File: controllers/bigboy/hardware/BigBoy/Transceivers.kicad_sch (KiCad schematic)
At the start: 15 parts, among them U13 74ALVC16245DG, U8 74ALVC16245DG

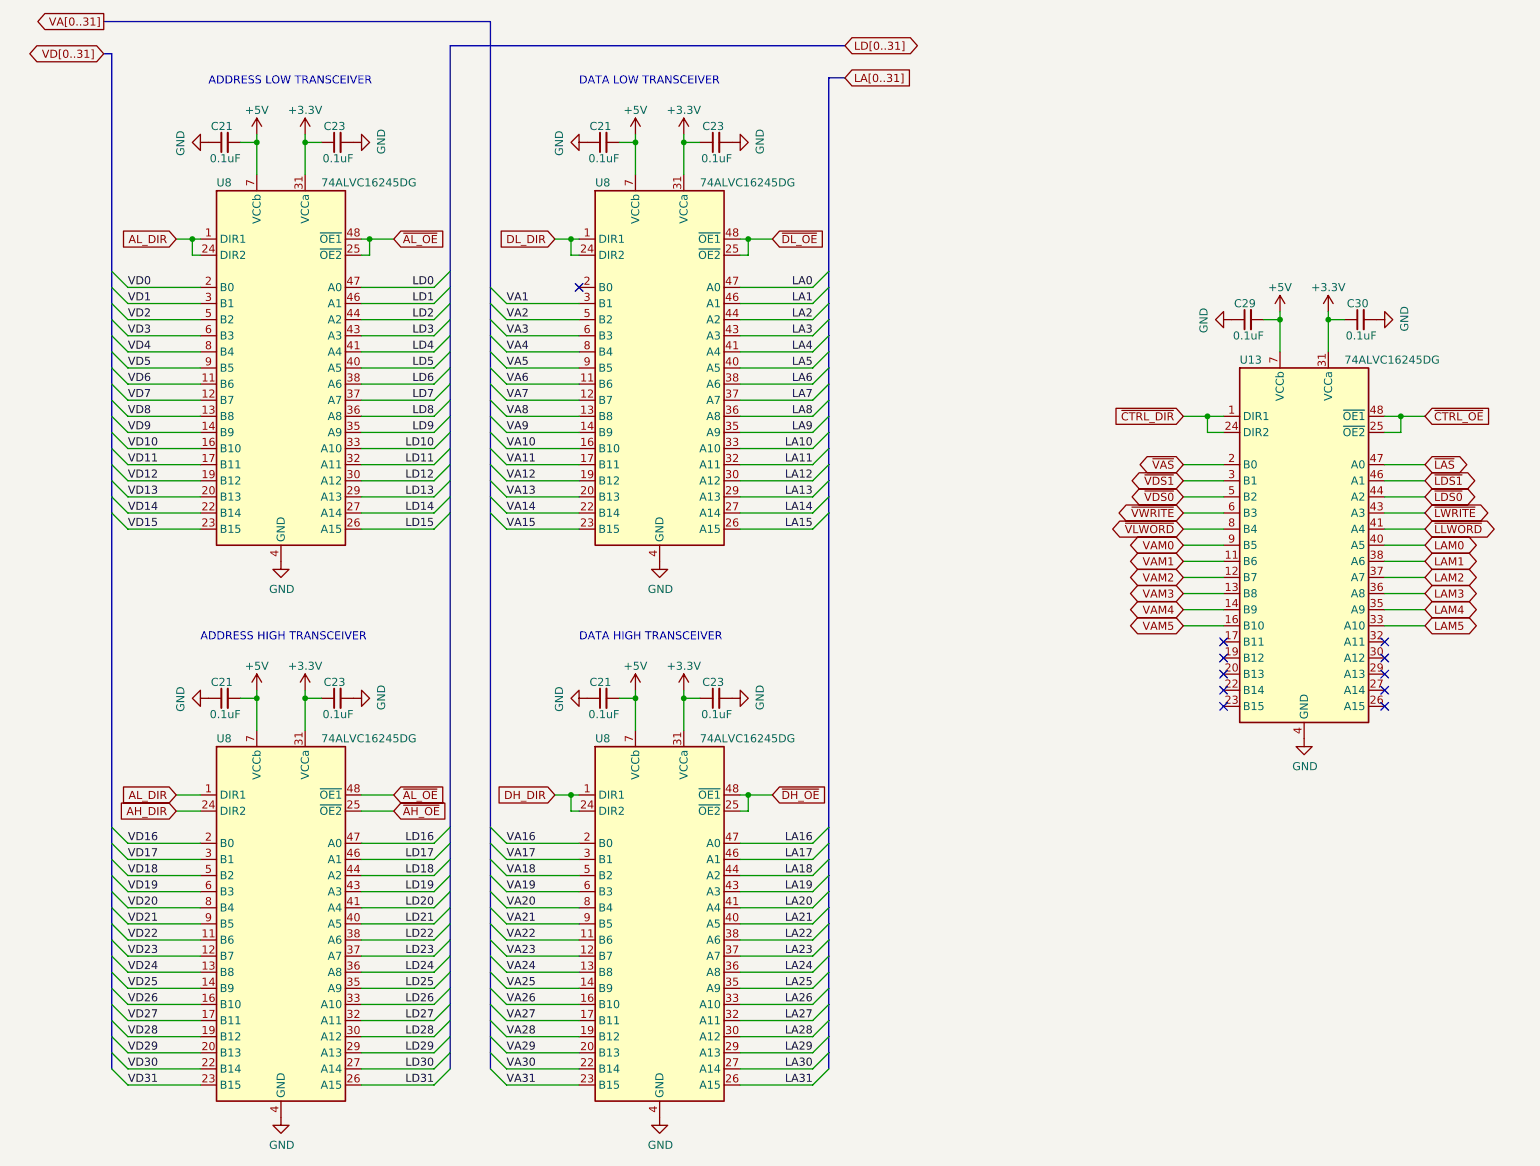
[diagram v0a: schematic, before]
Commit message: Reorganized to make it easier to group hardware and firmware files together
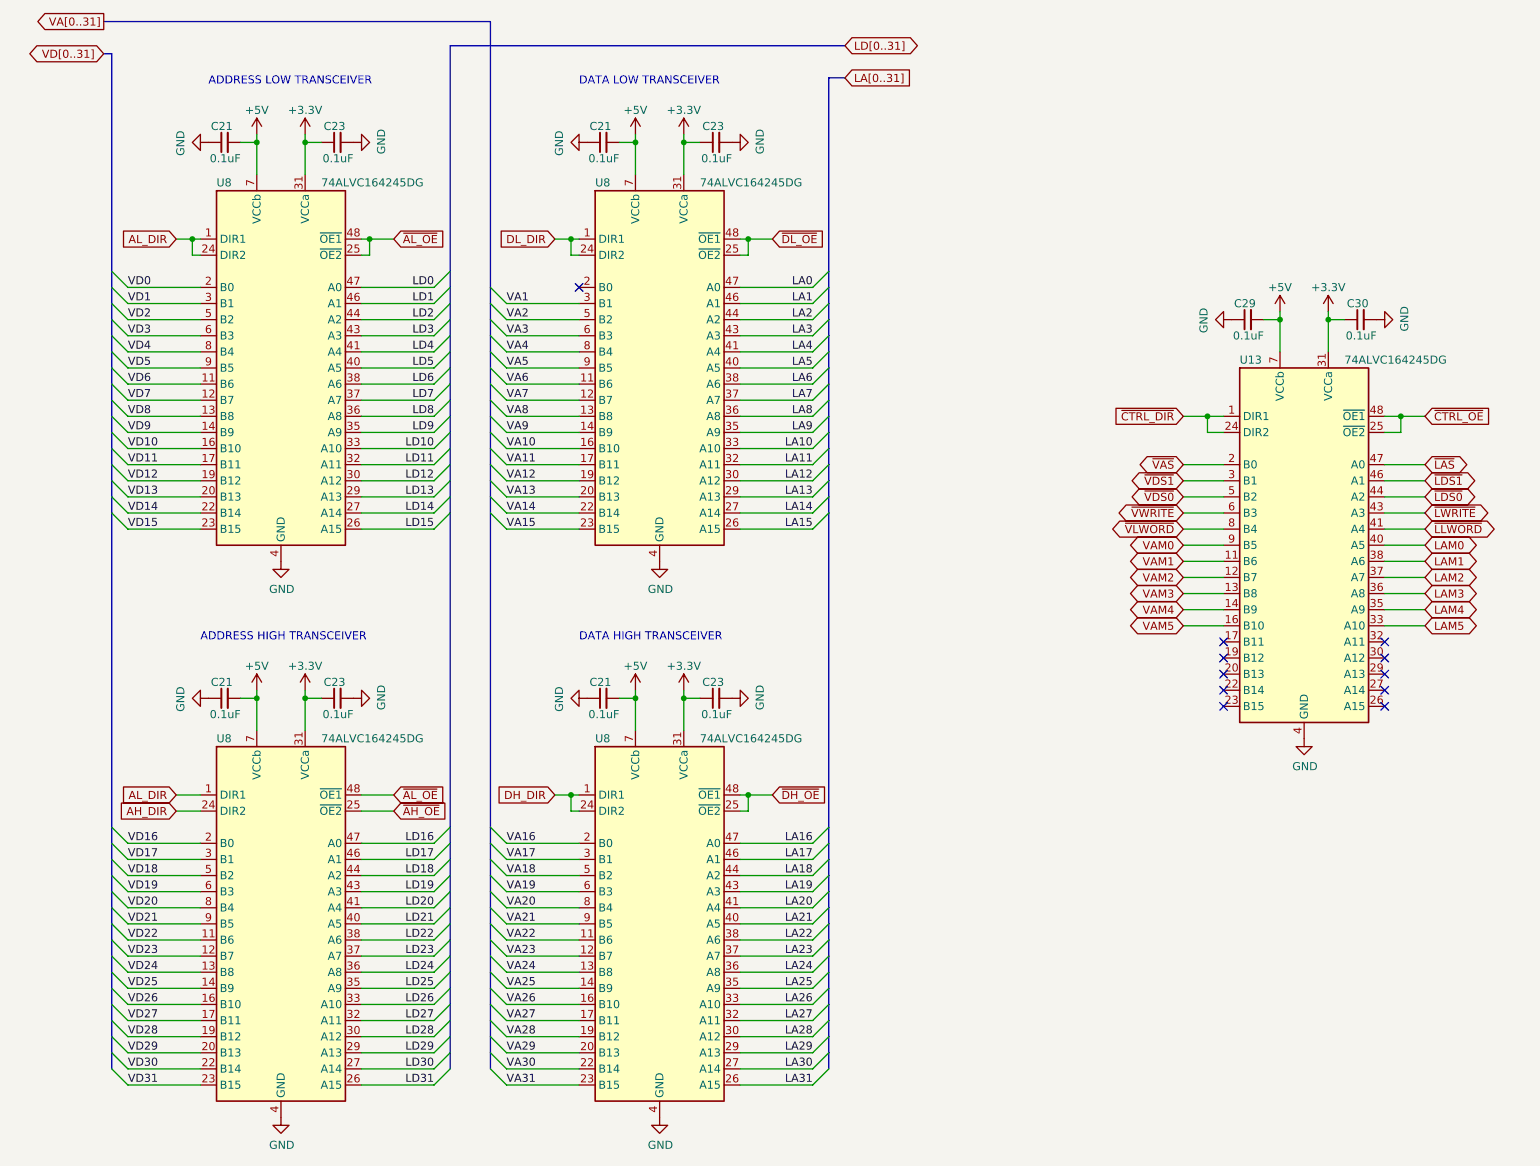
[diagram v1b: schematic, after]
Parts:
- U13, U8: value 74ALVC16245DG -> 74ALVC164245DG
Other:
- title: IVC-STH7 -> BigBoy
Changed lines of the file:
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@@
   (paper "A4")
   (title_block
-    (title "IVC-STH7")
+    (title "BigBoy")
     (rev "1")
   )
@@
         )
       )
-      (project "IVC-STH7"
+      (project "BigBoy"
         (path "/dd13a6b9-cb24-4a73-96ce-c29930072fba/d84460b0-5709-47d7-8f66-71b9360a0384"
           (reference "#PWR092") (unit 1)
@@
         )
       )
-      (project "IVC-STH7"
+      (project "BigBoy"
         (path "/dd13a6b9-cb24-4a73-96ce-c29930072fba/d84460b0-5709-47d7-8f66-71b9360a0384"
           (reference "#PWR086") (unit 1)
@@
         )
       )
-      (project "IVC-STH7"
+      (project "BigBoy"
         (path "/dd13a6b9-cb24-4a73-96ce-c29930072fba/d84460b0-5709-47d7-8f66-71b9360a0384"
           (reference "C35") (unit 1)
@@
         )
       )
-      (project "IVC-STH7"
+      (project "BigBoy"
         (path "/dd13a6b9-cb24-4a73-96ce-c29930072fba/d84460b0-5709-47d7-8f66-71b9360a0384"
           (reference "C36") (unit 1)
@@
       (effects (font (size 1.27 1.27)) (justify left))
     )
-    (property "Value" "74ALVC16245DG" (at 222.25 68.58 0)
+    (property "Value" "74ALVC164245DG" (at 222.25 68.58 0)
       (effects (font (size 1.27 1.27)) (justify left))
     )
@@
         )
       )
-      (project "IVC-STH7"
+      (project "BigBoy"
         (path "/dd13a6b9-cb24-4a73-96ce-c29930072fba/d84460b0-5709-47d7-8f66-71b9360a0384"
           (reference "U9") (unit 1)
@@
     (pin "1")
     (instances
-      (project "IVC-STH7"
+      (project "BigBoy"
         (path "/dd13a6b9-cb24-4a73-96ce-c29930072fba/dfc443dd-7c5d-4956-9c53-a8ea419d150b"
           (reference "#PWR081") (unit 1)
@@
         )
       )
-      (project "IVC-STH7"
+      (project "BigBoy"
         (path "/dd13a6b9-cb24-4a73-96ce-c29930072fba/69e17b68-518f-4a96-bc5f-1d2df7d01a56"
           (reference "#PWR032") (unit 1)
@@
         )
       )
-      (project "IVC-STH7"
+      (project "BigBoy"
         (path "/dd13a6b9-cb24-4a73-96ce-c29930072fba/69e17b68-518f-4a96-bc5f-1d2df7d01a56"
           (reference "#PWR032") (unit 1)
@@
         )
       )
-      (project "IVC-STH7"
+      (project "BigBoy"
         (path "/dd13a6b9-cb24-4a73-96ce-c29930072fba/d84460b0-5709-47d7-8f66-71b9360a0384"
           (reference "#PWR088") (unit 1)
@@
         )
       )
-      (project "IVC-STH7"
+      (project "BigBoy"
         (path "/dd13a6b9-cb24-4a73-96ce-c29930072fba/d84460b0-5709-47d7-8f66-71b9360a0384"
           (reference "#PWR070") (unit 1)
@@
         )
       )
-      (project "IVC-STH7"
+      (project "BigBoy"
         (path "/dd13a6b9-cb24-4a73-96ce-c29930072fba/d84460b0-5709-47d7-8f66-71b9360a0384"
           (reference "C37") (unit 1)
@@
         )
       )
-      (project "IVC-STH7"
+      (project "BigBoy"
         (path "/dd13a6b9-cb24-4a73-96ce-c29930072fba/d84460b0-5709-47d7-8f66-71b9360a0384"
           (reference "C43") (unit 1)
@@
     (pin "1")
     (instances
-      (project "IVC-STH7"
+      (project "BigBoy"
         (path "/dd13a6b9-cb24-4a73-96ce-c29930072fba/dfc443dd-7c5d-4956-9c53-a8ea419d150b"
           (reference "#PWR081") (unit 1)
@@
         )
       )
-      (project "IVC-STH7"
+      (project "BigBoy"
         (path "/dd13a6b9-cb24-4a73-96ce-c29930072fba/d84460b0-5709-47d7-8f66-71b9360a0384"
           (reference "C41") (unit 1)
@@
         )
       )
-      (project "IVC-STH7"
+      (project "BigBoy"
         (path "/dd13a6b9-cb24-4a73-96ce-c29930072fba/d84460b0-5709-47d7-8f66-71b9360a0384"
           (reference "#PWR077") (unit 1)
@@
         )
       )
-      (project "IVC-STH7"
+      (project "BigBoy"
         (path "/dd13a6b9-cb24-4a73-96ce-c29930072fba/d84460b0-5709-47d7-8f66-71b9360a0384"
           (reference "#PWR085") (unit 1)
@@
         )
       )
-      (project "IVC-STH7"
+      (project "BigBoy"
         (path "/dd13a6b9-cb24-4a73-96ce-c29930072fba/d84460b0-5709-47d7-8f66-71b9360a0384"
           (reference "C42") (unit 1)
@@
         )
       )
-      (project "IVC-STH7"
+      (project "BigBoy"
         (path "/dd13a6b9-cb24-4a73-96ce-c29930072fba/d84460b0-5709-47d7-8f66-71b9360a0384"
           (reference "#PWR076") (unit 1)
@@
       (effects (font (size 1.27 1.27)) (justify left))
     )
-    (property "Value" "74ALVC16245DG" (at 60.96 40.64 0)
+    (property "Value" "74ALVC164245DG" (at 60.96 40.64 0)
       (effects (font (size 1.27 1.27)) (justify left))
     )
@@
         )
       )
-      (project "IVC-STH7"
+      (project "BigBoy"
         (path "/dd13a6b9-cb24-4a73-96ce-c29930072fba/d84460b0-5709-47d7-8f66-71b9360a0384"
           (reference "U5") (unit 1)
@@
         )
       )
-      (project "IVC-STH7"
+      (project "BigBoy"
         (path "/dd13a6b9-cb24-4a73-96ce-c29930072fba/d84460b0-5709-47d7-8f66-71b9360a0384"
           (reference "#PWR093") (unit 1)
@@
         )
       )
-      (project "IVC-STH7"
+      (project "BigBoy"
         (path "/dd13a6b9-cb24-4a73-96ce-c29930072fba/d84460b0-5709-47d7-8f66-71b9360a0384"
           (reference "#PWR087") (unit 1)
@@
         )
       )
-      (project "IVC-STH7"
+      (project "BigBoy"
         (path "/dd13a6b9-cb24-4a73-96ce-c29930072fba/69e17b68-518f-4a96-bc5f-1d2df7d01a56"
           (reference "#PWR032") (unit 1)
@@
         )
       )
-      (project "IVC-STH7"
+      (project "BigBoy"
         (path "/dd13a6b9-cb24-4a73-96ce-c29930072fba/d84460b0-5709-47d7-8f66-71b9360a0384"
           (reference "#PWR075") (unit 1)
@@
     (pin "1")
     (instances
-      (project "IVC-STH7"
+      (project "BigBoy"
         (path "/dd13a6b9-cb24-4a73-96ce-c29930072fba/dfc443dd-7c5d-4956-9c53-a8ea419d150b"
           (reference "#PWR081") (unit 1)
@@
       (effects (font (size 1.27 1.27)) (justify left))
     )
-    (property "Value" "74ALVC16245DG" (at 120.65 40.64 0)
+    (property "Value" "74ALVC164245DG" (at 120.65 40.64 0)
       (effects (font (size 1.27 1.27)) (justify left))
     )
@@
         )
       )
-      (project "IVC-STH7"
+      (project "BigBoy"
         (path "/dd13a6b9-cb24-4a73-96ce-c29930072fba/d84460b0-5709-47d7-8f66-71b9360a0384"
           (reference "U7") (unit 1)
@@
     (pin "1")
     (instances
-      (project "IVC-STH7"
+      (project "BigBoy"
         (path "/dd13a6b9-cb24-4a73-96ce-c29930072fba/dfc443dd-7c5d-4956-9c53-a8ea419d150b"
           (reference "#PWR081") (unit 1)
@@
         )
       )
-      (project "IVC-STH7"
+      (project "BigBoy"
         (path "/dd13a6b9-cb24-4a73-96ce-c29930072fba/d84460b0-5709-47d7-8f66-71b9360a0384"
           (reference "#PWR069") (unit 1)
@@
       (effects (font (size 1.27 1.27)) (justify left))
     )
-    (property "Value" "74ALVC16245DG" (at 120.65 128.27 0)
+    (property "Value" "74ALVC164245DG" (at 120.65 128.27 0)
       (effects (font (size 1.27 1.27)) (justify left))
     )
@@
         )
       )
-      (project "IVC-STH7"
+      (project "BigBoy"
         (path "/dd13a6b9-cb24-4a73-96ce-c29930072fba/d84460b0-5709-47d7-8f66-71b9360a0384"
           (reference "U8") (unit 1)
@@
         )
       )
-      (project "IVC-STH7"
+      (project "BigBoy"
         (path "/dd13a6b9-cb24-4a73-96ce-c29930072fba/d84460b0-5709-47d7-8f66-71b9360a0384"
           (reference "C38") (unit 1)
@@
         )
       )
-      (project "IVC-STH7"
+      (project "BigBoy"
         (path "/dd13a6b9-cb24-4a73-96ce-c29930072fba/d84460b0-5709-47d7-8f66-71b9360a0384"
           (reference "C40") (unit 1)
@@
         )
       )
-      (project "IVC-STH7"
+      (project "BigBoy"
         (path "/dd13a6b9-cb24-4a73-96ce-c29930072fba/d84460b0-5709-47d7-8f66-71b9360a0384"
           (reference "C39") (unit 1)
@@
         )
       )
-      (project "IVC-STH7"
+      (project "BigBoy"
         (path "/dd13a6b9-cb24-4a73-96ce-c29930072fba/d84460b0-5709-47d7-8f66-71b9360a0384"
           (reference "#PWR080") (unit 1)
@@
         )
       )
-      (project "IVC-STH7"
+      (project "BigBoy"
         (path "/dd13a6b9-cb24-4a73-96ce-c29930072fba/69e17b68-518f-4a96-bc5f-1d2df7d01a56"
           (reference "#PWR032") (unit 1)
@@
       (effects (font (size 1.27 1.27)) (justify left))
     )
-    (property "Value" "74ALVC16245DG" (at 60.96 128.27 0)
+    (property "Value" "74ALVC164245DG" (at 60.96 128.27 0)
       (effects (font (size 1.27 1.27)) (justify left))
     )
@@
         )
       )
-      (project "IVC-STH7"
+      (project "BigBoy"
         (path "/dd13a6b9-cb24-4a73-96ce-c29930072fba/d84460b0-5709-47d7-8f66-71b9360a0384"
           (reference "U6") (unit 1)
@@
         )
       )
-      (project "IVC-STH7"
+      (project "BigBoy"
         (path "/dd13a6b9-cb24-4a73-96ce-c29930072fba/d84460b0-5709-47d7-8f66-71b9360a0384"
           (reference "#PWR089") (unit 1)
@@
         )
       )
-      (project "IVC-STH7"
+      (project "BigBoy"
         (path "/dd13a6b9-cb24-4a73-96ce-c29930072fba/d84460b0-5709-47d7-8f66-71b9360a0384"
           (reference "#PWR079") (unit 1)
@@
         )
       )
-      (project "IVC-STH7"
+      (project "BigBoy"
         (path "/dd13a6b9-cb24-4a73-96ce-c29930072fba/d84460b0-5709-47d7-8f66-71b9360a0384"
           (reference "#PWR078") (unit 1)
@@
         )
       )
-      (project "IVC-STH7"
+      (project "BigBoy"
         (path "/dd13a6b9-cb24-4a73-96ce-c29930072fba/d84460b0-5709-47d7-8f66-71b9360a0384"
           (reference "#PWR091") (unit 1)
@@
         )
       )
-      (project "IVC-STH7"
+      (project "BigBoy"
         (path "/dd13a6b9-cb24-4a73-96ce-c29930072fba/d84460b0-5709-47d7-8f66-71b9360a0384"
           (reference "C44") (unit 1)
@@
     (pin "1")
     (instances
-      (project "IVC-STH7"
+      (project "BigBoy"
         (path "/dd13a6b9-cb24-4a73-96ce-c29930072fba/dfc443dd-7c5d-4956-9c53-a8ea419d150b"
           (reference "#PWR081") (unit 1)
